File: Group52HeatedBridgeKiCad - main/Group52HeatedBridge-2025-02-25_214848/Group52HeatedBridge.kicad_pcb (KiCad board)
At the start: 2 copper layers, 24 parts, among them J1 UART, J10 TempSensorAirLED, J11 Regulator Vin, J2 RainSensor, J3 TemperatureSurface, J4 TemperatureAir, J5 JTAG, J6 TempSensorSurfaceLED, J7 RainSensor LED, J8 EN_BUTTON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

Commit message: power subsytem schematic push - second
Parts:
- removed J11: Regulator Vin, Connector_Molex:Molex_KK-254_AE-6410-02A_1x02_P2.54mm_Vertical
- added C4: 470uf, Capacitor_SMD:C_0805_2012Metric_Pad1.18x1.45mm_HandSolder, F.Cu at (249.4, 73.4)
- added C5: 330uf, Capacitor_SMD:C_0805_2012Metric_Pad1.18x1.45mm_HandSolder, F.Cu at (249.4, 76.4)
- added C6: 1uf, Capacitor_SMD:C_0805_2012Metric_Pad1.18x1.45mm_HandSolder, F.Cu at (249.4, 79.5)
- added D1: 1N5820, Diode_THT:D_DO-201AD_P3.81mm_Vertical_KathodeUp, F.Cu at (266.2, 56.9)
- added D2: 1N5820, Diode_THT:D_DO-201AD_P3.81mm_Vertical_KathodeUp, F.Cu at (261.3, 64.6)
- added J12: 54-00166, footprints_barrel:CONN3_54-00166_TEN, F.Cu at (252.2, 57.2)
- added J13: Heater1, Connector_Molex:Molex_KK-254_AE-6410-02A_1x02_P2.54mm_Vertical, F.Cu at (261.2, 71.9)
- added J14: Heater2, Connector_Molex:Molex_KK-254_AE-6410-02A_1x02_P2.54mm_Vertical, F.Cu at (268.3, 71.9)
- added L1: 47uh, Inductor_SMD:L_0805_2012Metric_Pad1.15x1.40mm_HandSolder, F.Cu at (254.2, 73.4)
- added R10: 10, Resistor_SMD:R_0805_2012Metric_Pad1.20x1.40mm_HandSolder, F.Cu at (254.2, 76.4)
- added R11: 10k, Resistor_SMD:R_0805_2012Metric_Pad1.20x1.40mm_HandSolder, F.Cu at (254.2, 79.3)
- added U2: XL1509-3.3, Package_SO:SOIC-8_3.9x4.9mm_P1.27mm, F.Cu at (280.4, 62.2)
- added U3: IRLZ44NPBF, footprints:PG-TO220-3_INF, F.Cu at (264.2, 79.5)
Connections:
- U1 pad 11: unconnected-(U1-IO26-Pad11) -> /MOSFETCONTROL
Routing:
- removed copper zone on B.Cu, net GND
- removed copper zone on F.Cu, net GND
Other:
- board outline added: 5.8 x 6.2 mm

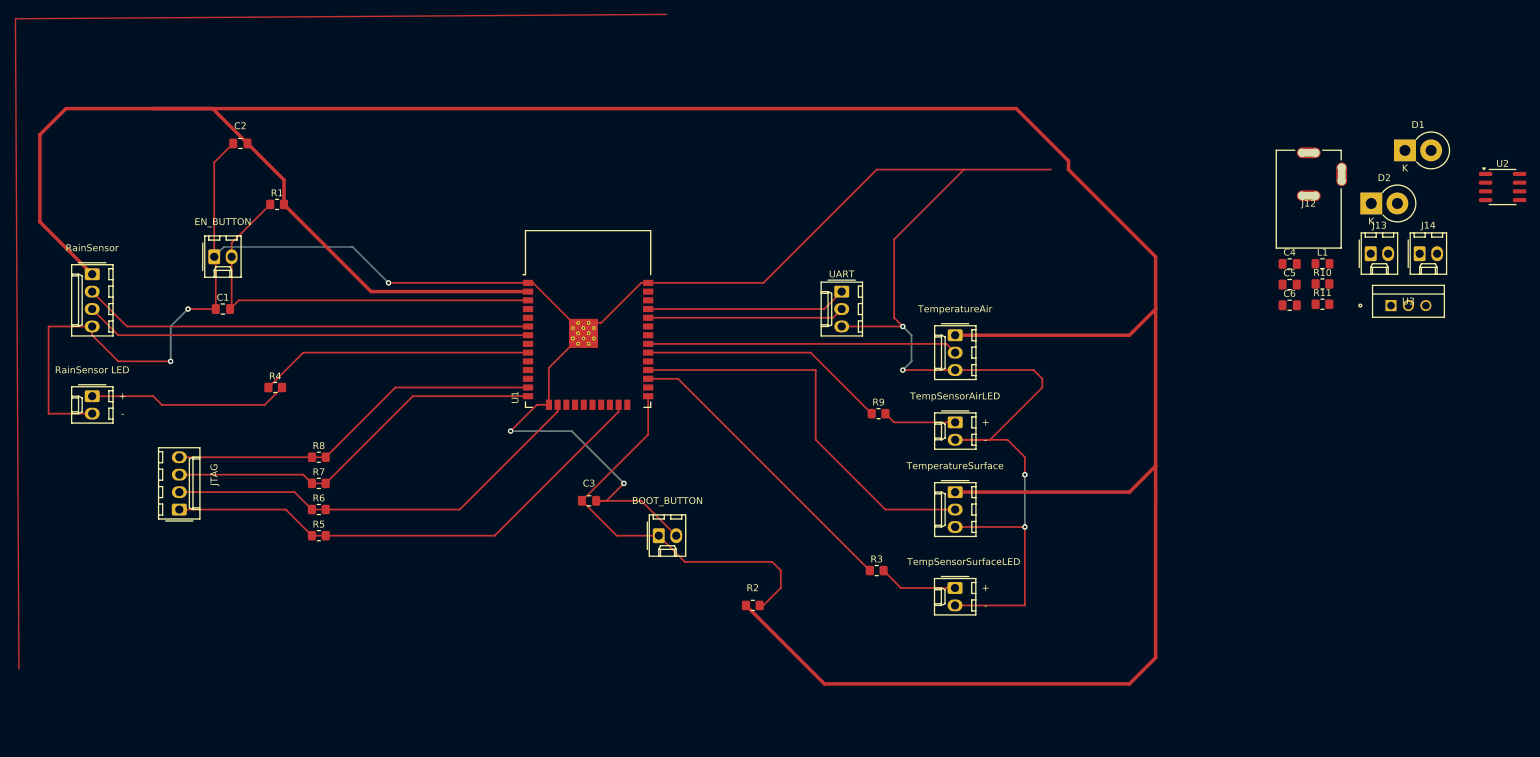
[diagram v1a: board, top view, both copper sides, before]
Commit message: resized schematic and cleaned up
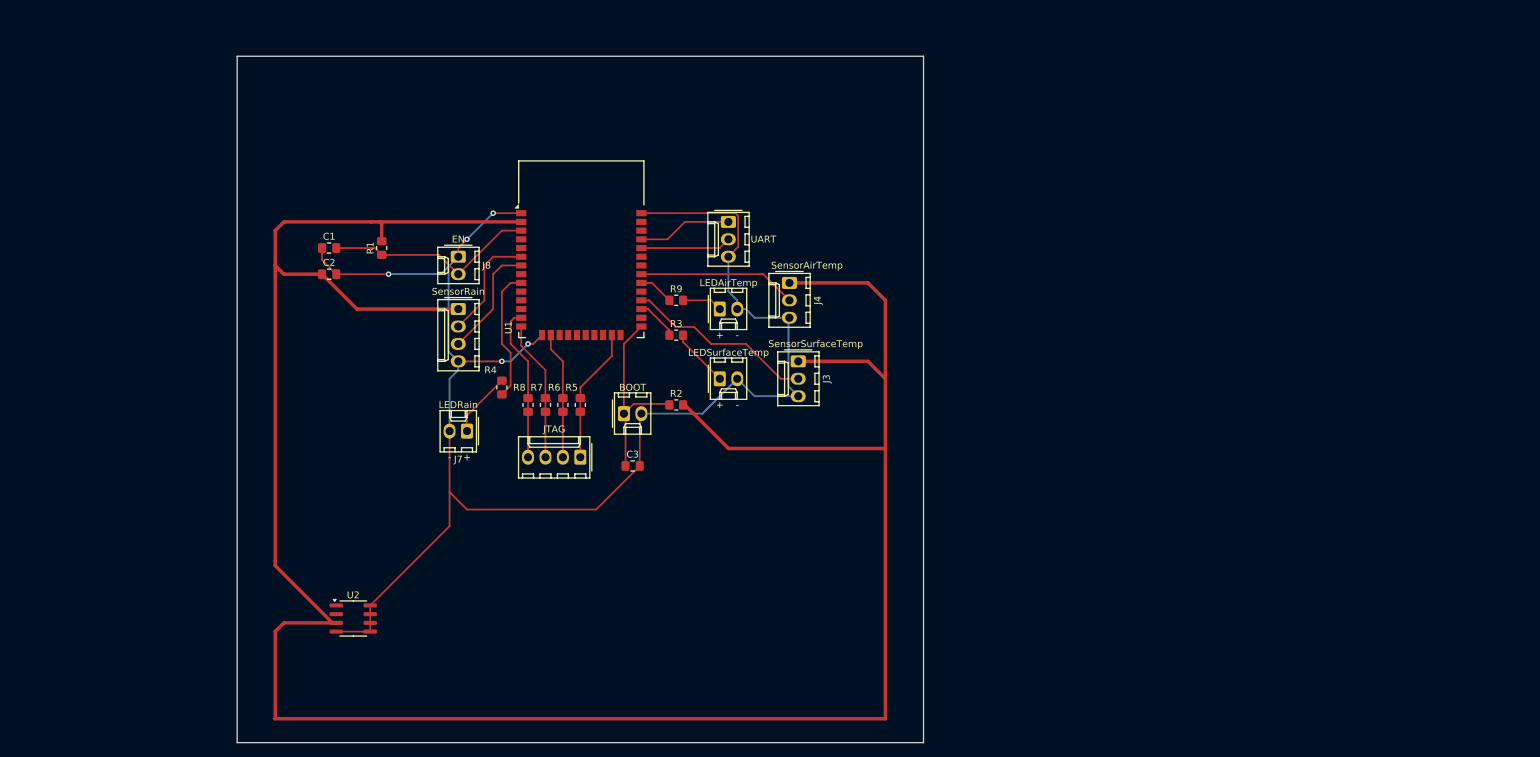
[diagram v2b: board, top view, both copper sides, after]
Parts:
- removed C4: 470uf, Capacitor_SMD:C_0805_2012Metric_Pad1.18x1.45mm_HandSolder
- removed C5: 330uf, Capacitor_SMD:C_0805_2012Metric_Pad1.18x1.45mm_HandSolder
- removed C6: 1uf, Capacitor_SMD:C_0805_2012Metric_Pad1.18x1.45mm_HandSolder
- removed D1, D2: 1N5820, Diode_THT:D_DO-201AD_P3.81mm_Vertical_KathodeUp
- removed J12: 54-00166, footprints_barrel:CONN3_54-00166_TEN
- removed J13: Heater1, Connector_Molex:Molex_KK-254_AE-6410-02A_1x02_P2.54mm_Vertical
- removed J14: Heater2, Connector_Molex:Molex_KK-254_AE-6410-02A_1x02_P2.54mm_Vertical
- removed L1: 47uh, Inductor_SMD:L_0805_2012Metric_Pad1.15x1.40mm_HandSolder
- removed R10: 10, Resistor_SMD:R_0805_2012Metric_Pad1.20x1.40mm_HandSolder
- removed R11: 10k, Resistor_SMD:R_0805_2012Metric_Pad1.20x1.40mm_HandSolder
- removed U3: IRLZ44NPBF, footprints:PG-TO220-3_INF
- moved U2 178.9 mm to (113.0, 125.1)
- moved J5 58.9 mm to (146.1, 101.6), turned to 180 degrees
- moved J7 54.8 mm to (129.5, 97.8), turned to 180 degrees
- moved J2 53.6 mm to (128.3, 80.0)
- moved J6 45.9 mm to (166.4, 90.2), turned to 0 degrees
- moved R3 45.0 mm to (160.0, 83.8)
- moved R5 42.6 mm to (146.1, 94.0), turned to 90 degrees
- moved R6 38.7 mm to (143.5, 94.0), turned to 90 degrees
- moved J10 38.1 mm to (166.4, 80.0), turned to 0 degrees
- moved J8 35.6 mm to (128.3, 72.4), turned to -90 degrees
- moved R7 34.9 mm to (141.0, 94.0), turned to 90 degrees
- moved R9 33.8 mm to (160.0, 78.7)
- moved R4 33.0 mm to (134.6, 91.4), turned to 90 degrees
- moved R8 31.4 mm to (138.4, 94.0), turned to 90 degrees
- moved R2 31.3 mm to (160.0, 94.0), turned to 0 degrees
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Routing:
- net GND: track 404.5 -> 229.4 mm, vias 9 -> 5
- net +3.3V: track 451.1 -> 362.6 mm
- net /MTDO: track 74.1 -> 19.7 mm
- net /DigitalRain: track 65.6 -> 16.4 mm
- net /AnalogRain: track 65.1 -> 16.9 mm
- net /MTCK: track 63.1 -> 18.5 mm
- net /GPIOTempSurfaceLED: track 43.9 -> 6.07 mm
- net /MTDI: track 56.6 -> 20.5 mm
- net /MTMS: track 55.0 -> 22.6 mm
- net /GPIOTempSurface: track 59.1 -> 27.6 mm
- net /GPIOTempAirLED: track 36.3 -> 5.13 mm
- net /EN: track 61.6 -> 31.2 mm
- net /BOOT: track 59.1 -> 28.7 mm
- net /GPIOTempAir: track 45.3 -> 23.1 mm
- net /GPIORainLED: track 39.9 -> 19.4 mm
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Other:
- board size 5.8 x 6.2 mm -> 100 x 100 mm

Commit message: B Revert "resized schematic and cleaned up"
This reverts commit bab35e5b8986f5439bb45f55d315508e4487ff8d.

reverted auto save file
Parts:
- added C4: 470uf, Capacitor_SMD:C_0805_2012Metric_Pad1.18x1.45mm_HandSolder, F.Cu at (249.4, 73.4)
- added C5: 330uf, Capacitor_SMD:C_0805_2012Metric_Pad1.18x1.45mm_HandSolder, F.Cu at (249.4, 76.4)
- added C6: 1uf, Capacitor_SMD:C_0805_2012Metric_Pad1.18x1.45mm_HandSolder, F.Cu at (249.4, 79.5)
- added D1: 1N5820, Diode_THT:D_DO-201AD_P3.81mm_Vertical_KathodeUp, F.Cu at (266.2, 56.9)
- added D2: 1N5820, Diode_THT:D_DO-201AD_P3.81mm_Vertical_KathodeUp, F.Cu at (261.3, 64.6)
- added J12: 54-00166, footprints_barrel:CONN3_54-00166_TEN, F.Cu at (252.2, 57.2)
- added J13: Heater1, Connector_Molex:Molex_KK-254_AE-6410-02A_1x02_P2.54mm_Vertical, F.Cu at (261.2, 71.9)
- added J14: Heater2, Connector_Molex:Molex_KK-254_AE-6410-02A_1x02_P2.54mm_Vertical, F.Cu at (268.3, 71.9)
- added L1: 47uh, Inductor_SMD:L_0805_2012Metric_Pad1.15x1.40mm_HandSolder, F.Cu at (254.2, 73.4)
- added R10: 10, Resistor_SMD:R_0805_2012Metric_Pad1.20x1.40mm_HandSolder, F.Cu at (254.2, 76.4)
- added R11: 10k, Resistor_SMD:R_0805_2012Metric_Pad1.20x1.40mm_HandSolder, F.Cu at (254.2, 79.3)
- added U3: IRLZ44NPBF, footprints:PG-TO220-3_INF, F.Cu at (264.2, 79.5)
- moved U2 178.9 mm to (280.4, 62.2)
- moved J5 58.9 mm to (87.6, 109.2), turned to 90 degrees
- moved J7 54.8 mm to (74.9, 92.7), turned to -90 degrees
- moved J2 53.6 mm to (74.9, 74.9)
- moved J6 45.9 mm to (200.6, 120.7), turned to -90 degrees
- moved R3 45.0 mm to (189.2, 118.1)
- moved R5 42.6 mm to (108.0, 113.0), turned to 0 degrees
- moved R6 38.7 mm to (108.0, 109.2), turned to 0 degrees
- moved J10 38.1 mm to (200.7, 96.5), turned to -90 degrees
- moved J8 35.6 mm to (92.7, 72.4), turned to 0 degrees
- moved R7 34.9 mm to (108.0, 105.4), turned to 0 degrees
- moved R9 33.8 mm to (189.5, 95.2)
- moved R4 33.0 mm to (101.6, 91.4), turned to 0 degrees
- moved R8 31.4 mm to (108.0, 101.6), turned to 0 degrees
- moved R2 31.3 mm to (171.2, 123.2), turned to 180 degrees
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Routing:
- net GND: track 229.4 -> 404.5 mm, vias 5 -> 9
- net +3.3V: track 362.6 -> 451.1 mm
- net /MTDO: track 19.7 -> 74.1 mm
- net /DigitalRain: track 16.4 -> 65.6 mm
- net /AnalogRain: track 16.9 -> 65.1 mm
- net /MTCK: track 18.5 -> 63.1 mm
- net /GPIOTempSurfaceLED: track 6.07 -> 43.9 mm
- net /MTDI: track 20.5 -> 56.6 mm
- net /MTMS: track 22.6 -> 55.0 mm
- net /GPIOTempSurface: track 27.6 -> 59.1 mm
- net /GPIOTempAirLED: track 5.13 -> 36.3 mm
- net /EN: track 31.2 -> 61.6 mm
- net /BOOT: track 28.7 -> 59.1 mm
- net /GPIOTempAir: track 23.1 -> 45.3 mm
- net /GPIORainLED: track 19.4 -> 39.9 mm
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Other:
- board size 100 x 100 mm -> 5.8 x 6.2 mm
